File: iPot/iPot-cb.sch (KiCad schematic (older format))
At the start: 28 parts, among them IC1 ATMEGA644-P, P1 JTAG, P10 SPRAY_PUMP, P11 USB_PWR, P2 SPI, P3 UART, P4 SOIL, P5 TEMP/HUMID, P6 LIGHT, P7 WATER_TANK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

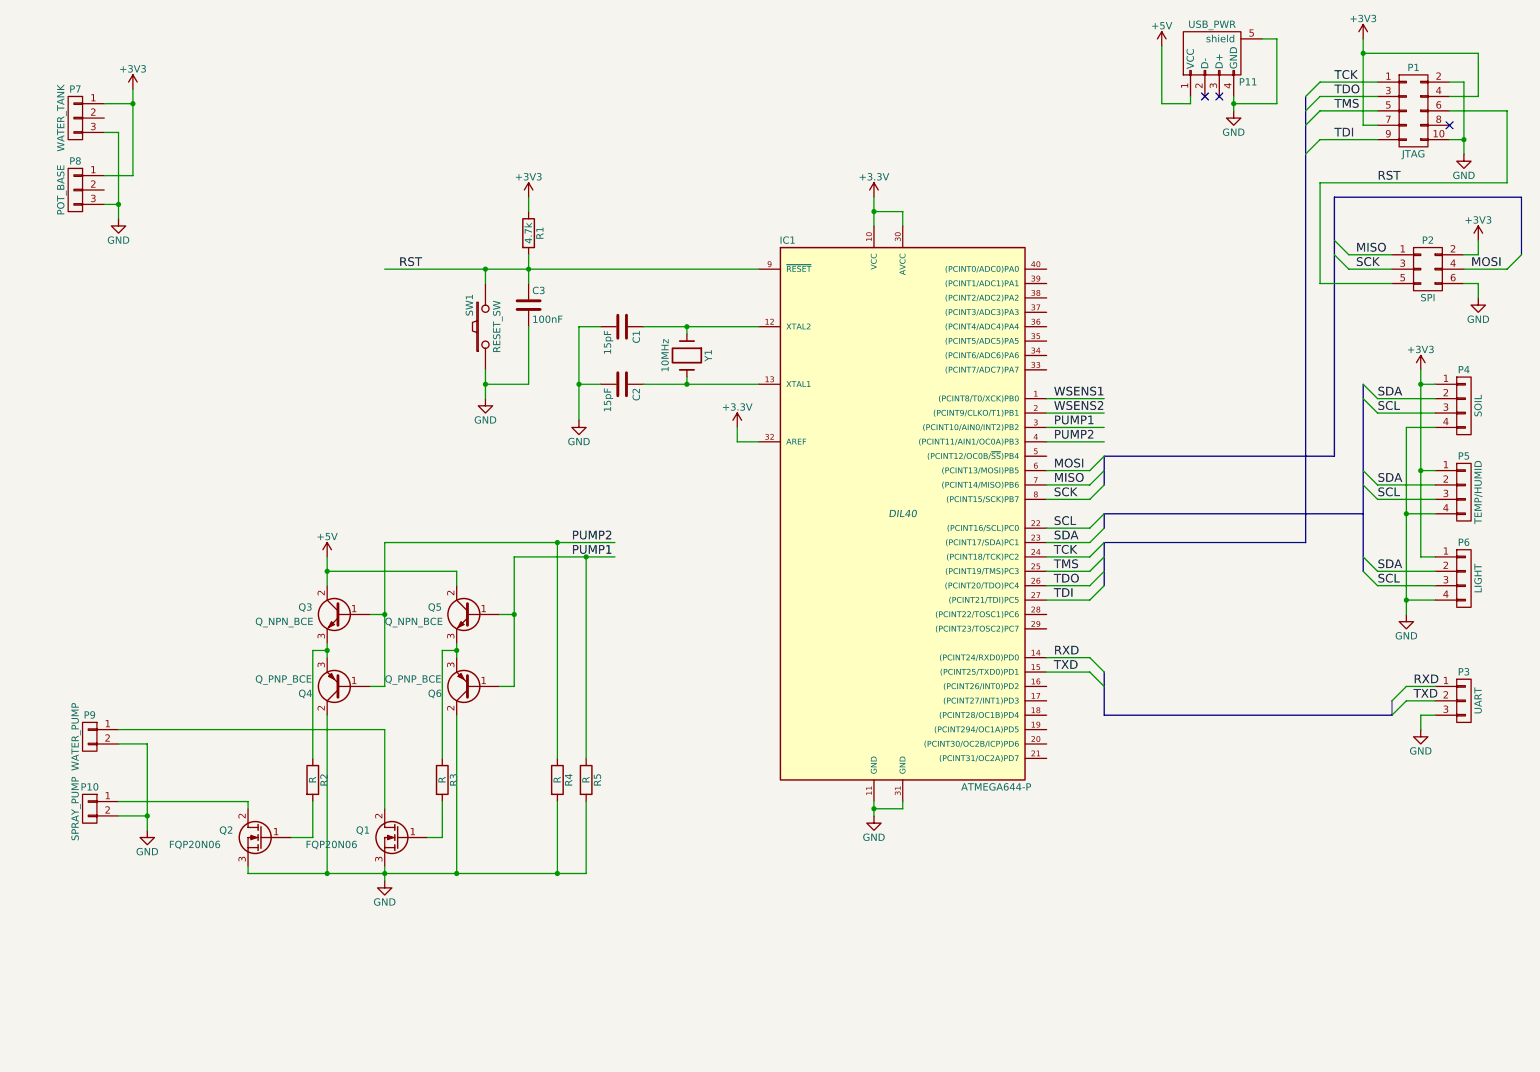
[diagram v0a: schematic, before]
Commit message: Complete circuit with TR placeholder.
TODO: Need to find correct TRs.
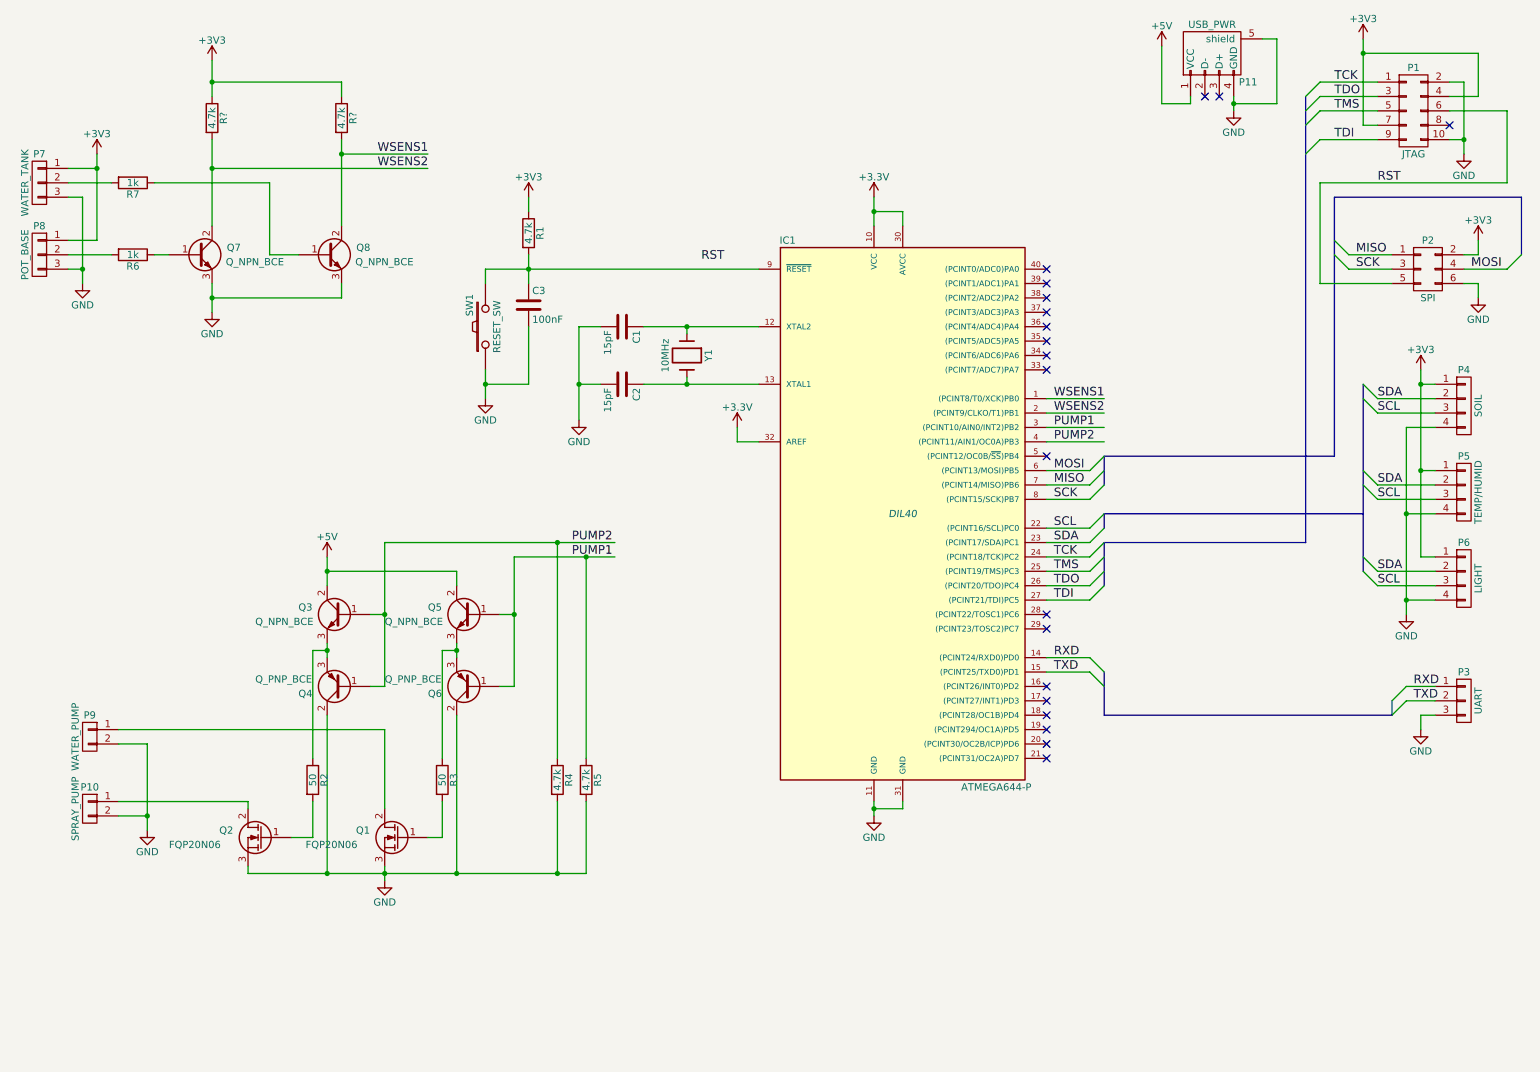
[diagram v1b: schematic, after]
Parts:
- added Q7, Q8: Q_NPN_BCE, symbol Q_NPN_BCE
- added R6, R7: 1k, symbol R
- added R? (x2): 4.7k, symbol R
- R2, R3: value R -> 50
- R4, R5: value R -> 4.7k
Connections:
- wire segments 129 -> 145
- no-connect marks 3 -> 20
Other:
- moved on the sheet: P7, P8

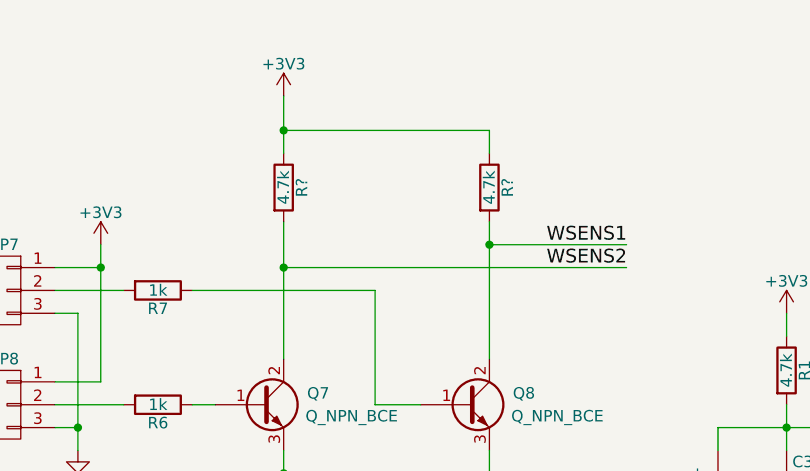
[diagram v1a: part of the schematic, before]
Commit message: Add resistor label
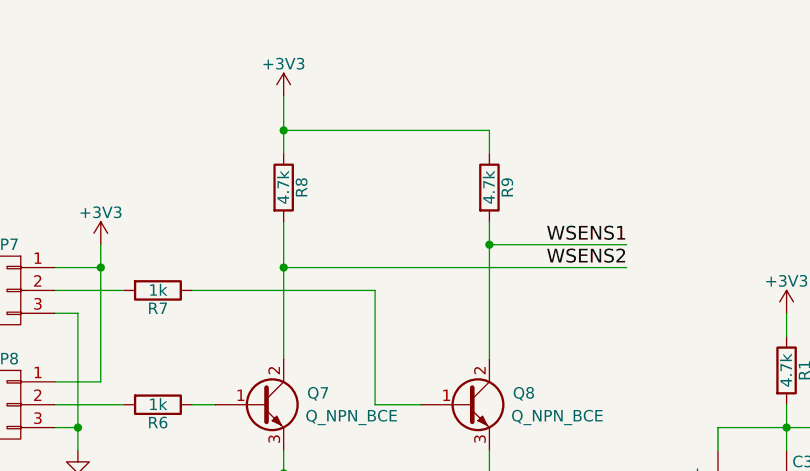
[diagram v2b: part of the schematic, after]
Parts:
- gave numbers to parts that had none: 2
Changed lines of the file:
@@
 $EndComp
 $Comp
-L R R?
+L R R8
 U 1 1 57287DCA
 P 1900 1250
-F 0 "R?" V 1980 1250 50  0000 C CNN
+F 0 "R8" V 1980 1250 50  0000 C CNN
 F 1 "4.7k" V 1900 1250 50  0000 C CNN
 F 2 "" V 1830 1250 50  0000 C CNN
@@
 $EndComp
 $Comp
-L R R?
+L R R9
 U 1 1 57287E98
 P 2800 1250
-F 0 "R?" V 2880 1250 50  0000 C CNN
+F 0 "R9" V 2880 1250 50  0000 C CNN
 F 1 "4.7k" V 2800 1250 50  0000 C CNN
 F 2 "" V 2730 1250 50  0000 C CNN

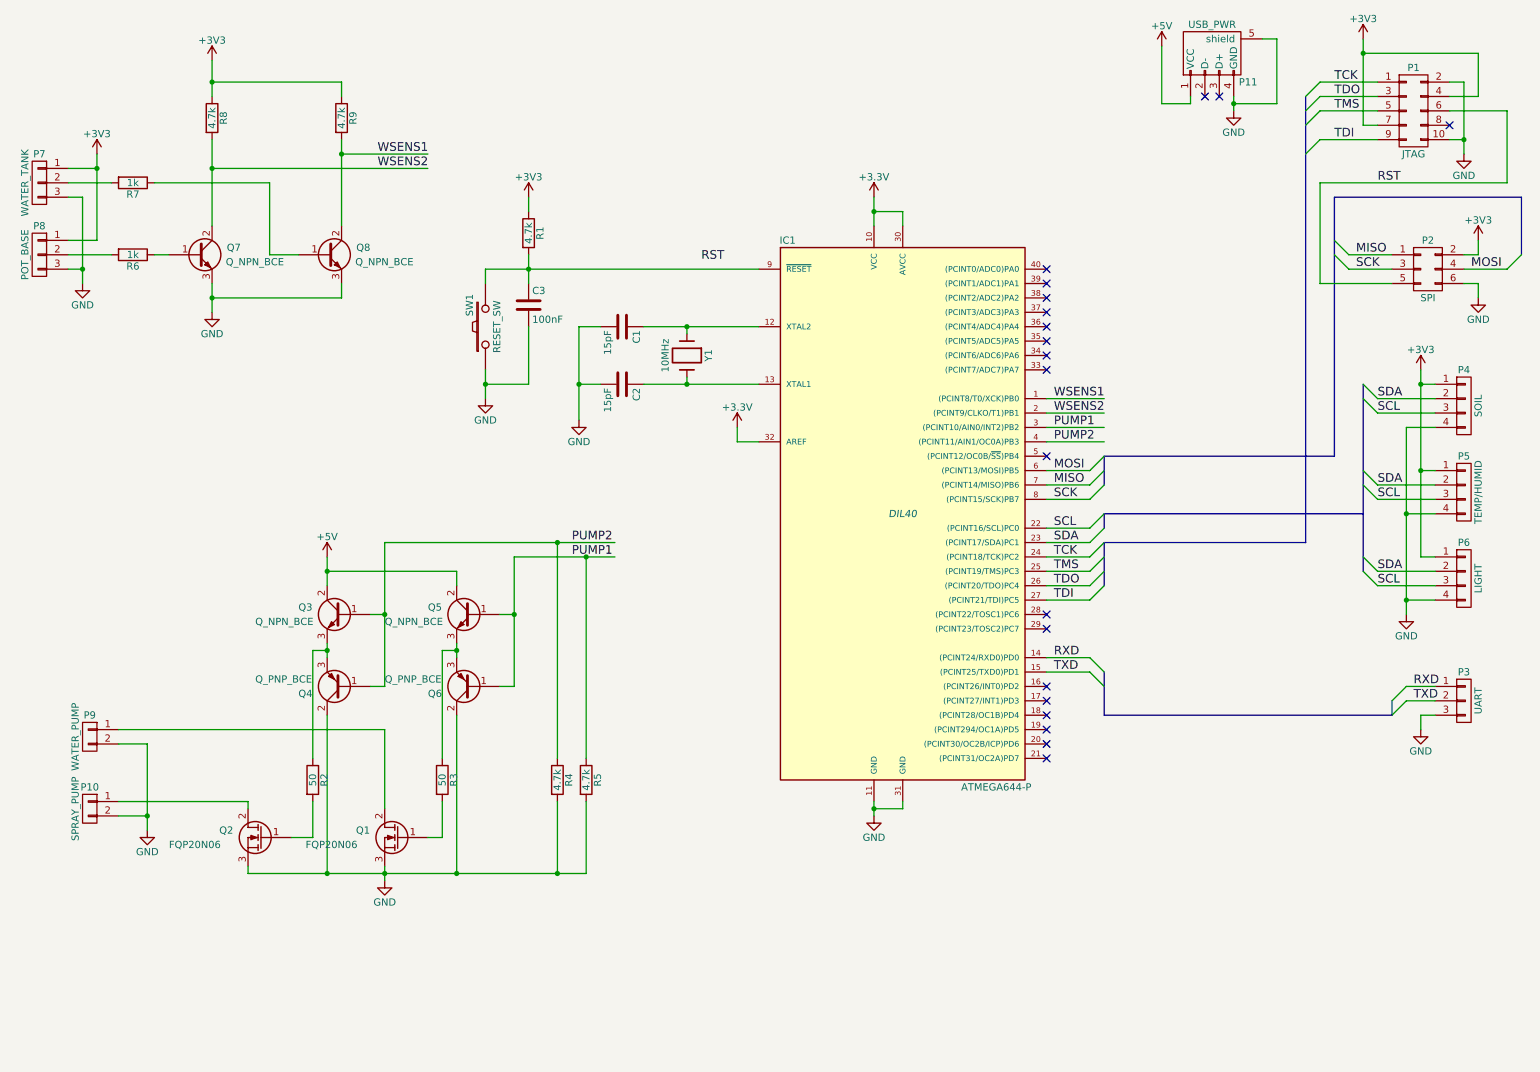
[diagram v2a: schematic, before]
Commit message: Draw some power regulators (WIP), Assign some footprint
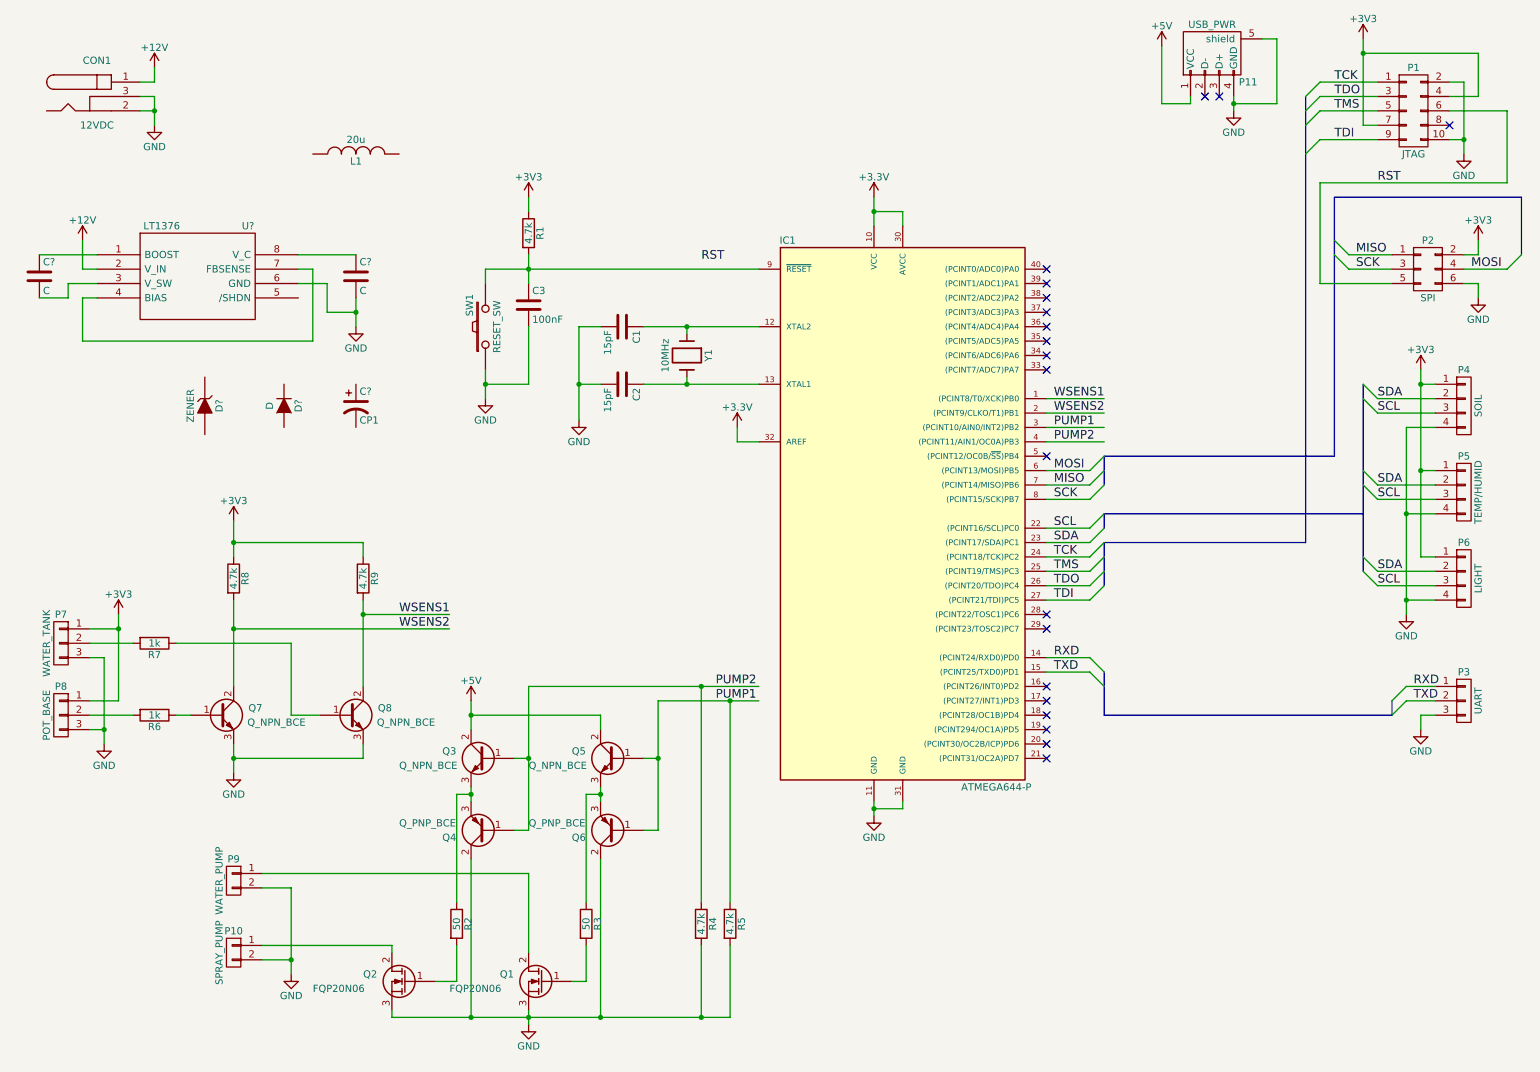
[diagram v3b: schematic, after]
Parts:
- added C? (x2): C, symbol C
- added C?: CP1, symbol CP1
- added CON1: 12VDC, Connect:BARREL_JACK, symbol BARREL_JACK
- added D?: ZENER, symbol ZENER
- added D?: D, symbol D
- added L1: 20u, symbol INDUCTOR
- added U?: LT1376, symbol LT1376
- IC1: footprint DIL40 -> Housings_DIP:DIP-40_W15.24mm
- P1: footprint (none) -> Pin_Headers:Pin_Header_Straight_2x05
- P11: footprint (none) -> Connect:USB_A
- P2: footprint (none) -> Pin_Headers:Pin_Header_Straight_2x03
- P3, P7, P8: footprint (none) -> Pin_Headers:Pin_Header_Straight_1x03
- SW1: footprint (none) -> Buttons_Switches_ThroughHole:SW_PUSH_SMALL
- Y1: footprint (none) -> Crystals:Crystal_HC49-U_Vertical
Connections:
- net labels added: +12V
- wire segments 145 -> 166
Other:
- moved on the sheet: P10, P7, P8, P9, Q1, Q2, Q3, Q4, Q5, Q6, Q7, Q8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

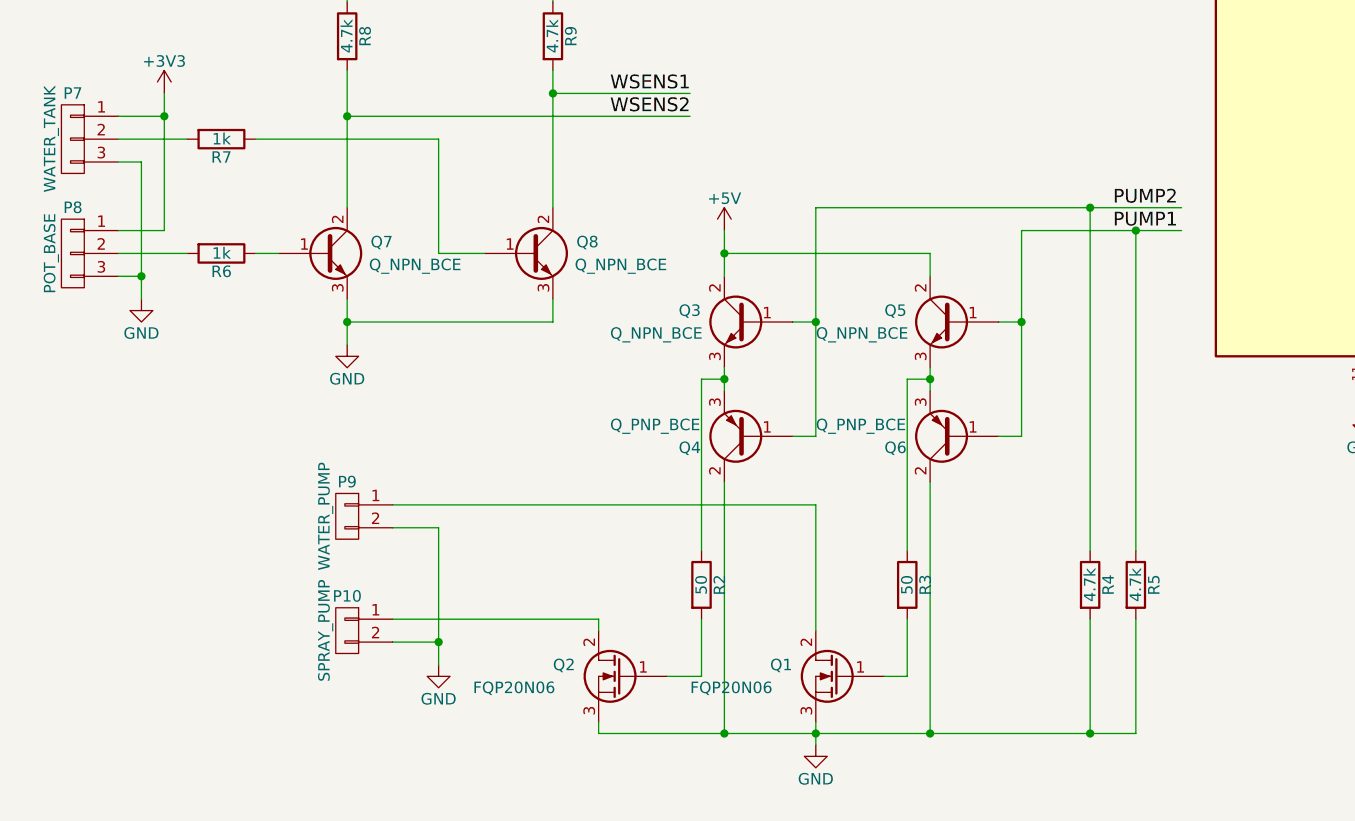
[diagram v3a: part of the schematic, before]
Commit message: Fix MOSFET driver
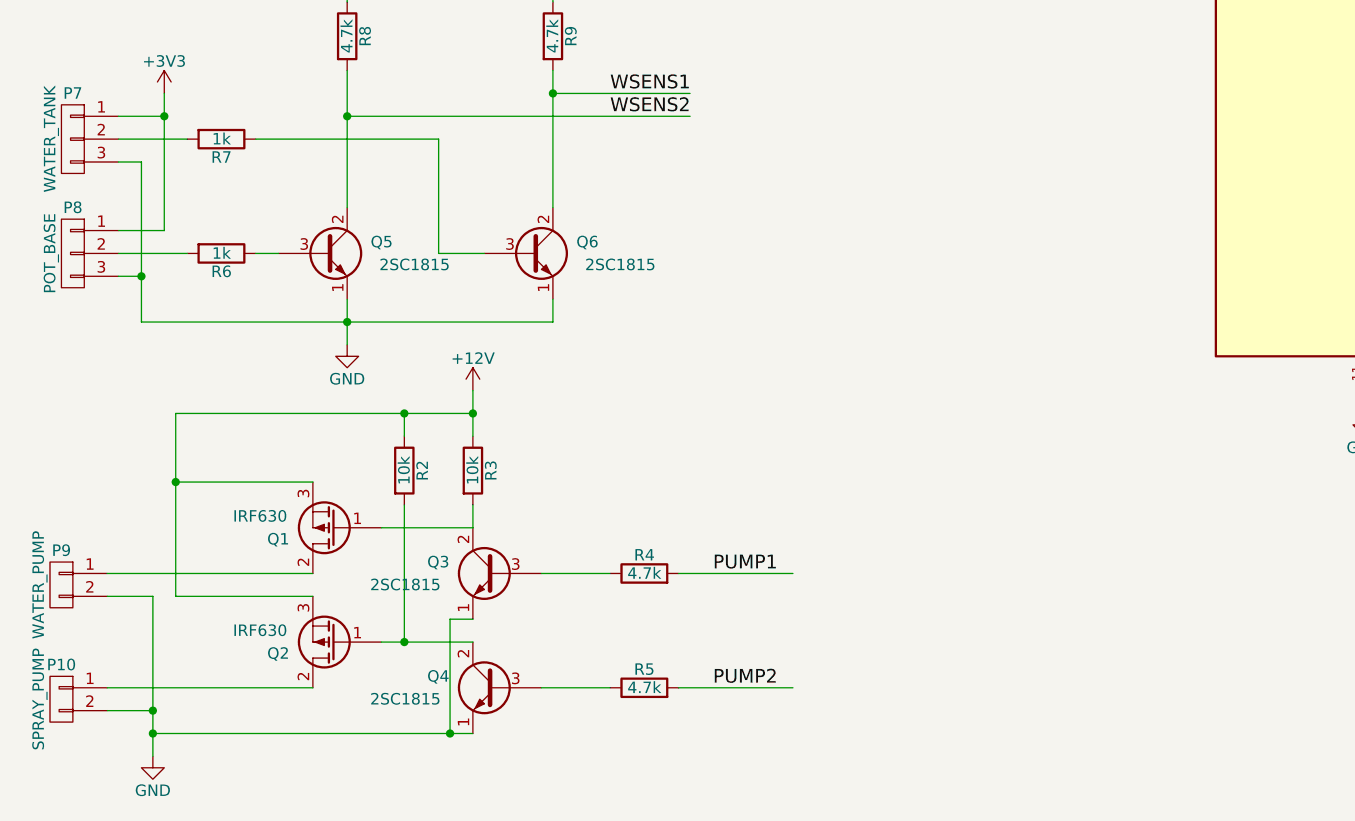
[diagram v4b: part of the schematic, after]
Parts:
- removed Q1, Q2: FQP20N06, symbol Q_NMOS_GDS
- removed Q3, Q5, Q7, Q8: Q_NPN_BCE, symbol Q_NPN_BCE
- removed Q4, Q6: Q_PNP_BCE, symbol Q_PNP_BCE
- added Q1, Q2: IRF630, symbol Q_PMOS_GDS
- added Q3, Q4, Q5, Q6: 2SC1815, symbol Q_NPN_ECB
- R2, R3: value 50 -> 10k
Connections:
- wire segments 166 -> 151
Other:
- moved on the sheet: P10, P9, R2, R3, R4, R5

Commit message: Design draft complete
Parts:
- added R?: 410, symbol R
- added R?: 250, symbol R
- added U2: LM317AT, TO-220, symbol LM317AT
- C?: value C -> 0.1u
- C?: value C -> 3.3n
- C?: value CP1 -> 100u
- D?: value ZENER -> 1N5818
- D?: value D -> 1N914
- gave numbers to parts that had none: 1
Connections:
- wire segments 151 -> 207
- no-connect marks 20 -> 21
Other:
- moved on the sheet: C?, CON1, D?, L1, U1

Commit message: Add annotation
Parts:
- gave numbers to parts that had none: 7
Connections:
- wire segments 207 -> 166
